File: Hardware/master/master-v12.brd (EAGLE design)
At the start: 58 x 61.2 mm, 48 parts, among them J1 22-05-7028-02

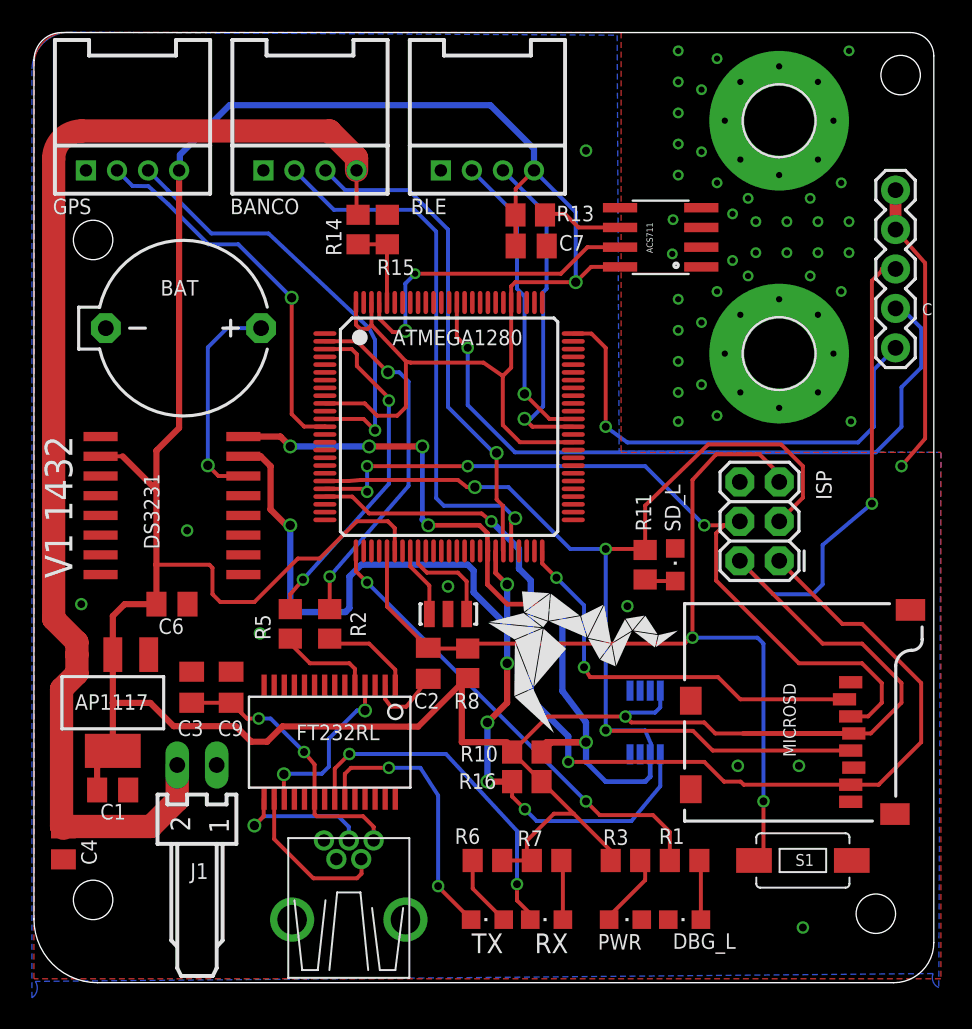
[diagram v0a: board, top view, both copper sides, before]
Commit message: V12
corrección Labels y pistas
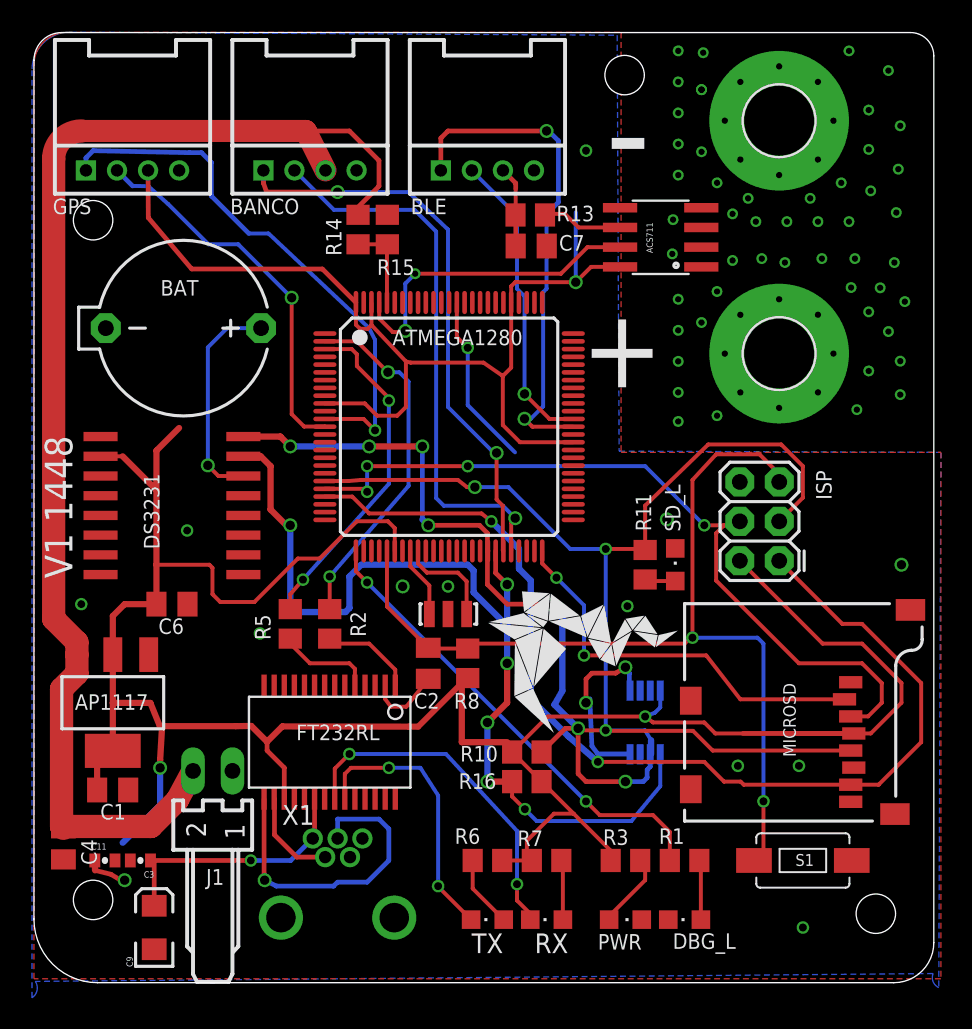
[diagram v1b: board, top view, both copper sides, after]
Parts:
- removed C: (no value), SparkFun-Connectors:1X05
- removed JP1: USB-MB-H, SparkFun-Connectors:USB-MB-H
- added C11: 0.1uF, SparkFun:0402-CAP
- added X1: USB-MB-H, SparkFun:USB-MB-H
- C3: value 10uF -> 0.1uF; device rcl:C0805K -> SparkFun:0402-CAP
- C9: value 0.1uF -> 10uF; device rcl:C0805K -> SparkFun:EIA3216
- moved C9 16.3 mm to (7.75, 3.30)
- moved C3 11.6 mm to (6.86, 7.62), turned to 180 degrees
- moved J1 1.09 mm to (11.5, 13.4)
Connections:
- net N$71 renamed IP+
- net N$72 renamed IP-
- net RX_GPS renamed GPS_RX
- removed net N$19: FT232RL.16, JP1.D-
- removed net N$24: C3.1, C9.1, FT232RL.20, JP1.VBUS
- removed net N$25: FT232RL.17, FT232RL.4
- removed net N$5: FT232RL.15, JP1.D+
- removed net TX_GPS: ATMEGA1280.12, GPS.3
- new net GPS_TX: ATMEGA1280.12, GPS.1
- new net USB_D+1: FT232RL.15, X1.D+
- new net USB_D-1: FT232RL.16, X1.D-
- new net VCC1: C3.1, C9.A, FT232RL.20, X1.VBUS
- new net VCCIO: FT232RL.4
- net 3.3V: now also BLE.3, C11.1, FT232RL.17, GPS.3; no longer BLE.4, C.3, GPS.4
- net AUX_CURRENT: no longer C.2
- net AUX_FAULT: no longer C.1
- net BT_TX: now also BLE.1; no longer BLE.3
- net COMM_TX: now also BANCO.1; no longer BANCO.3
- net GND: now also BANCO.4, BLE.4, C11.2, C9.C, GPS.4, X1.GND; no longer BANCO.1, BLE.1, C.4, C.5, C9.2, GPS.1, JP1.GND
- net RAW: now also BANCO.3; no longer BANCO.4
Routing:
- net 3.3V: track 293.7 -> 249.2 mm, vias 3 -> 4
- net GPS_TX: track 0.00 -> 35.3 mm, vias 0 -> 1
- net AUX_CURRENT: track 45.8 -> 11.2 mm
- net AUX_FAULT: track 31.2 -> 0.00 mm, vias 1 -> 0
- net TX_GPS: track 28.6 -> 0.00 mm, vias 1 -> 0
- net USB_D+1: track 0.00 -> 20.9 mm, vias 0 -> 1
- net N$24: track 18.7 -> 0.00 mm, vias 2 -> 0
- net VCC1: track 0.00 -> 16.8 mm, vias 0 -> 1
- net N$25: track 11.2 -> 0.00 mm, vias 2 -> 0
- net BT_TX: track 21.3 -> 32.5 mm, vias 1 -> 2
- net N$19: track 10.3 -> 0.00 mm
- net N$5: track 9.46 -> 0.00 mm, vias 1 -> 0
- net GND: track 19.1 -> 12.0 mm, vias 10 -> 14
- net USB_D-1: track 0.00 -> 6.18 mm
- net RAW: track 79.6 -> 84.3 mm
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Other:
- board text added: "+"
- board text added: "-"
- board text added: "V1 1448"
- board text removed: "V1 1432"
